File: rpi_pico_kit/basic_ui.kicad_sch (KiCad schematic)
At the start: 30 parts, among them Q3 BSS138, Q4 BSS138, Q5 BSS138, Q6 BSS138, SW2 RotaryEncoder_Switch

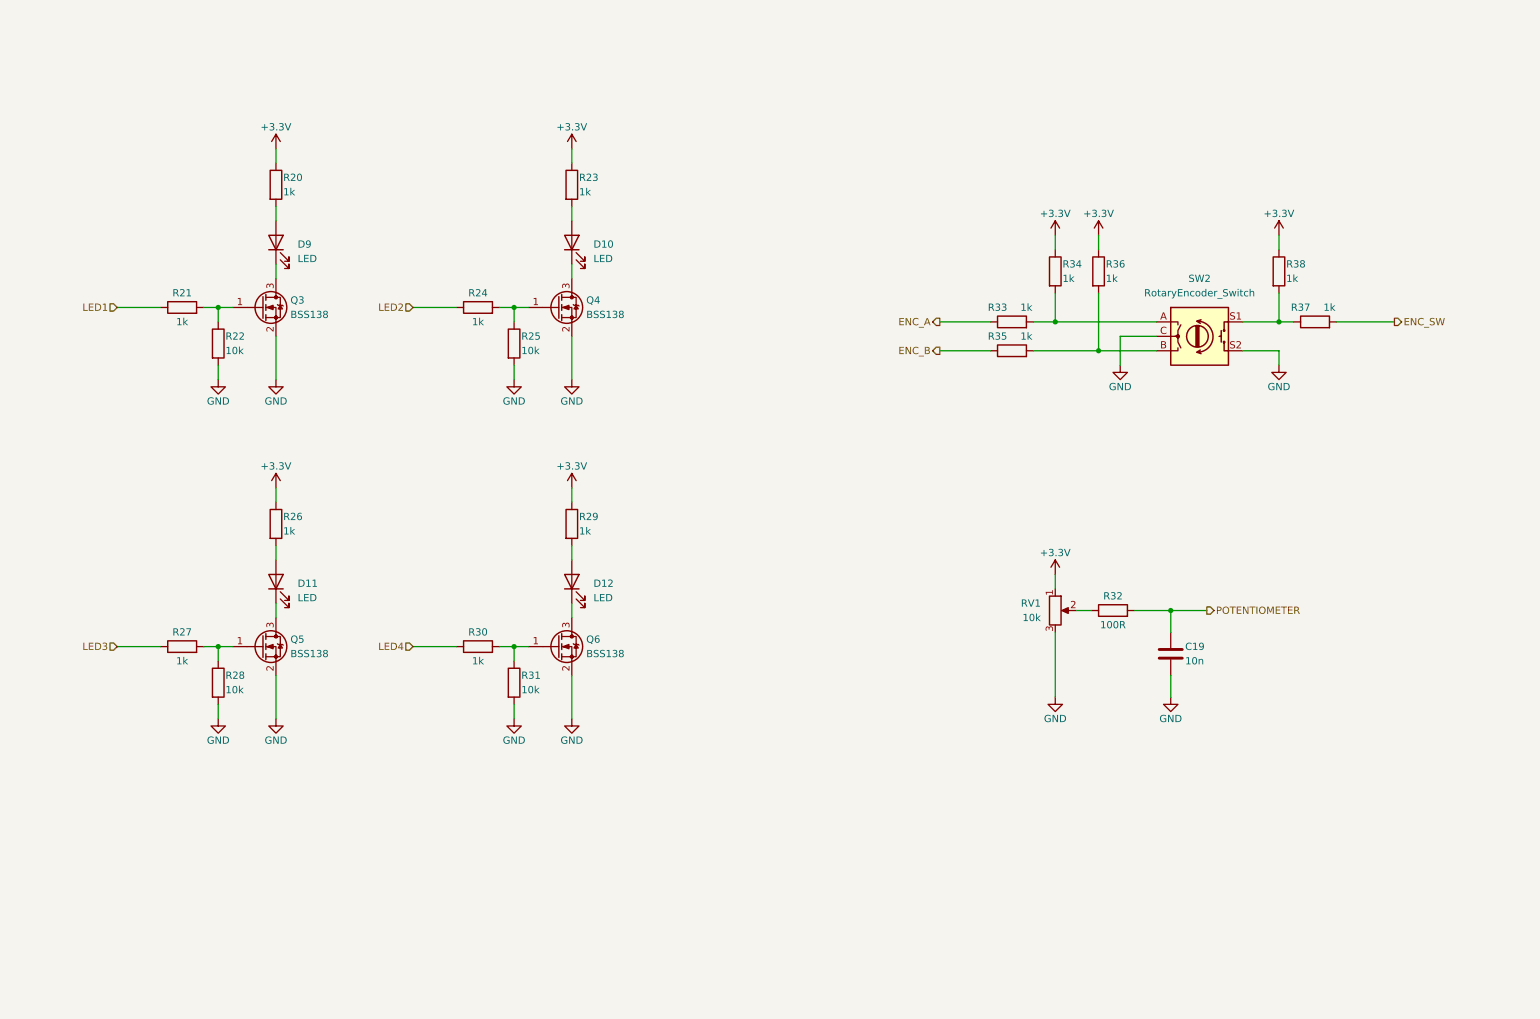
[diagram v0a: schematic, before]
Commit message: added dac buttons
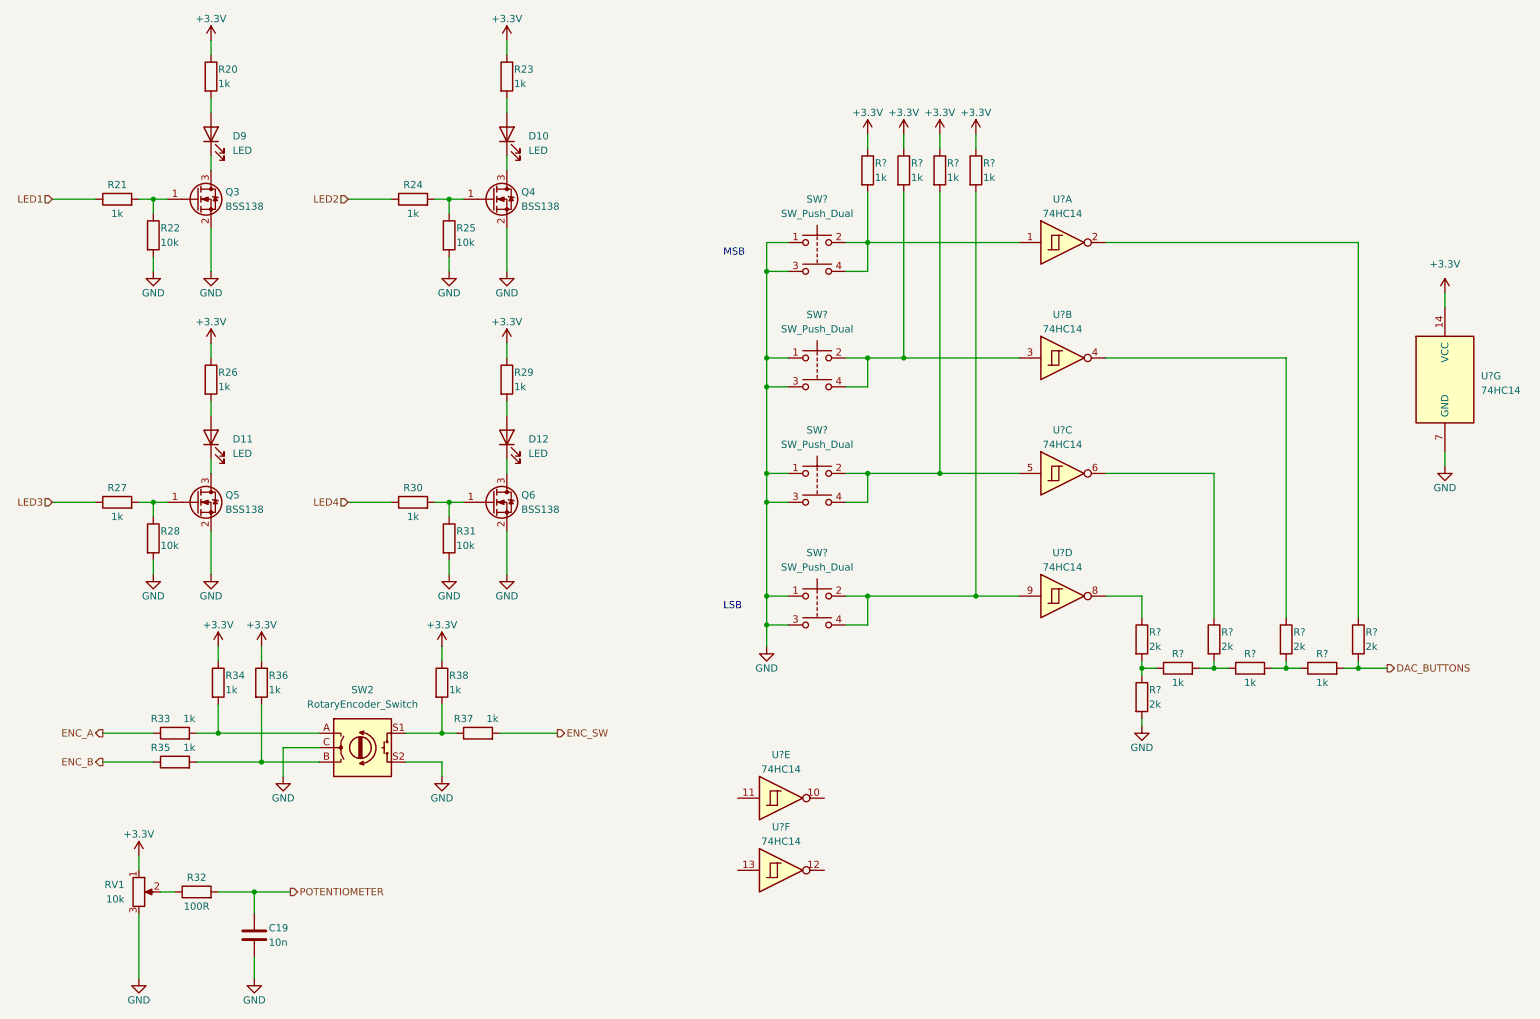
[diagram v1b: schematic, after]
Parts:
- added R? (x5): 2k, Resistor_SMD:R_0805_2012Metric_Pad1.20x1.40mm_HandSolder, symbol Device:R
- added R? (x7): 1k, Resistor_SMD:R_0805_2012Metric_Pad1.20x1.40mm_HandSolder, symbol Device:R
- added SW? (x4): SW_Push_Dual, symbol Switch:SW_Push_Dual
- added U? (x7): 74HC14, symbol 74xx:74HC14
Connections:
- net +3V3: now also R?.1, R?.1, R?.1, R?.1, U?.14 (VCC)
- net GND: now also R?.2, SW?.1, SW?.1, SW?.1, SW?.1, SW?.3, SW?.3, SW?.3, SW?.3, U?.7 (GND)
- new net: R?.2, SW?.2, SW?.4, U?.9
- new net: R?.1, U?.6
- new net: R?.1, R?.2, R?.2 (x2)
- new net: R?.2, SW?.2, SW?.4, U?.3
- new net: R?.1, U?.4
- new net: R?.1, R?.1, R?.2
- new net: R?.1, U?.8
- new net: R?.2, SW?.2, SW?.4, U?.1
- new net: R?.2, SW?.2, SW?.4, U?.5
- new net: R?.1, U?.2
- new net DAC_BUTTONS: R?.2, R?.2
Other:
- note added: "LSB"
- note added: "MSB"
- moved on the sheet: C19, D10, D11, D12, D9, Q3, Q4, Q5, Q6, R20, R21, R22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

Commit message: replaced spi expander
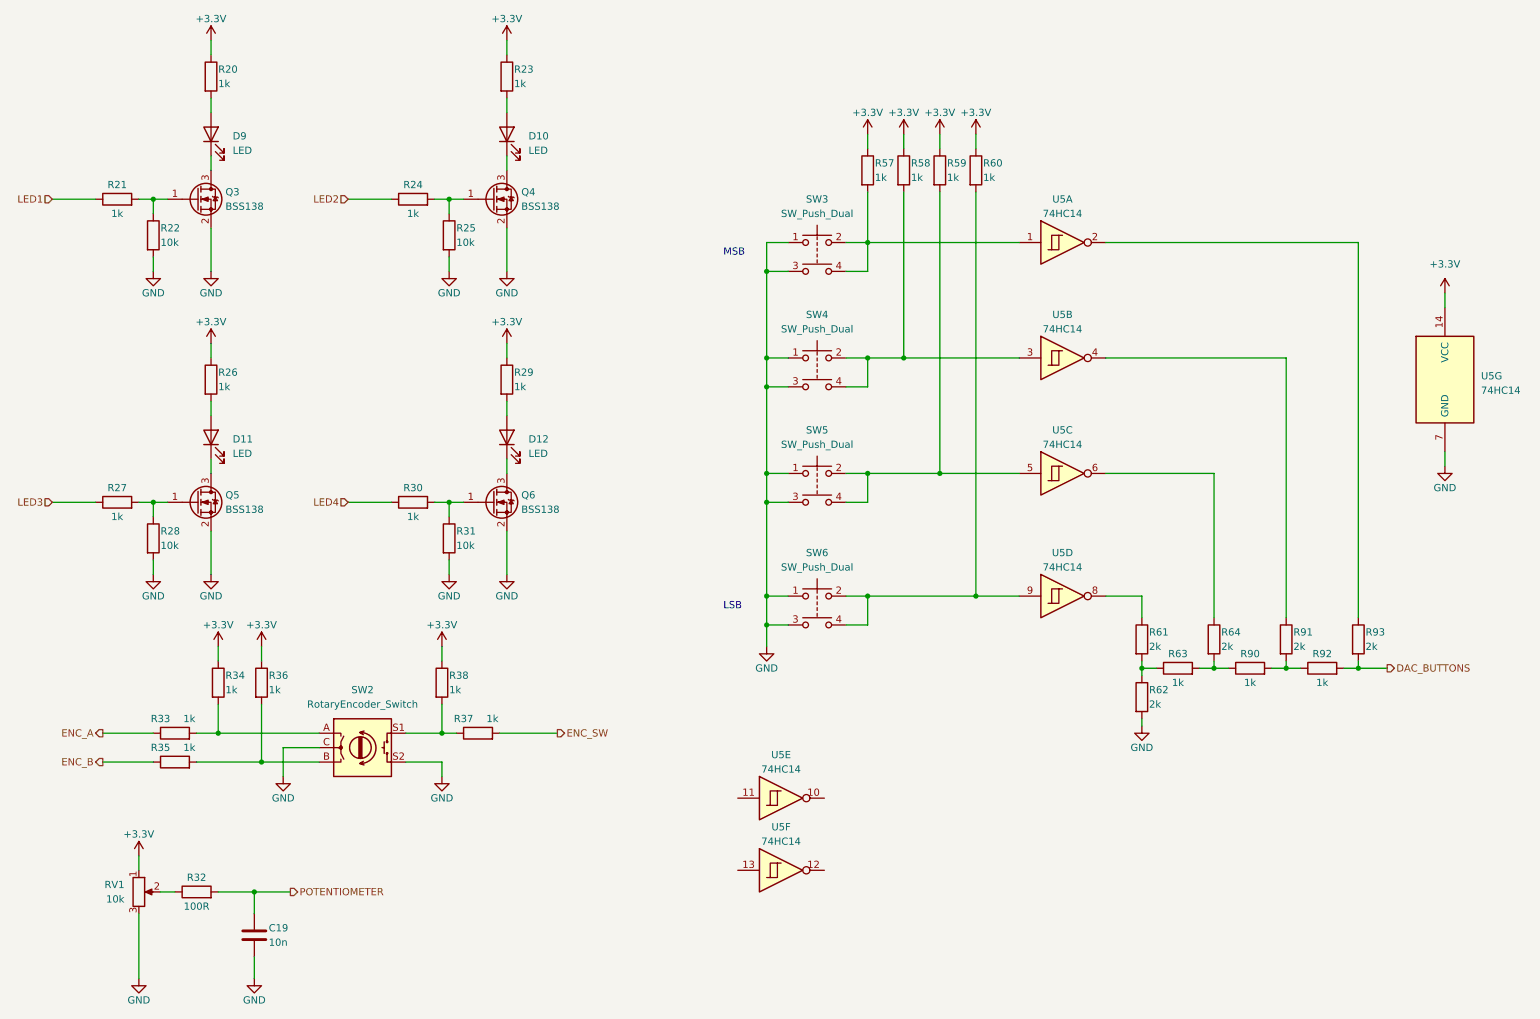
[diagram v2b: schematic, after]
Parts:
- gave numbers to parts that had none: 17
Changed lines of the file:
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@@
   (symbol (lib_id "Switch:SW_Push_Dual") (at 157.48 118.11 0) (unit 1)
     (in_bom yes) (on_board yes) (fields_autoplaced)
-    (property "Reference" "SW?" (id 0) (at 157.48 110.49 0)
+    (property "Reference" "SW6" (id 0) (at 157.48 110.49 0)
       (effects (font (size 1.27 1.27)))
     )
@@
   (symbol (lib_id "Device:R") (at 227.33 125.73 0) (unit 1)
     (in_bom yes) (on_board yes)
-    (property "Reference" "R?" (id 0) (at 228.6 124.46 0)
+    (property "Reference" "R64" (id 0) (at 228.6 124.46 0)
       (effects (font (size 1.27 1.27)) (justify left))
     )
@@
   (symbol (lib_id "power:GND") (at 148.59 127 0) (unit 1)
     (in_bom yes) (on_board yes)
-    (property "Reference" "#PWR?" (id 0) (at 148.59 133.35 0)
+    (property "Reference" "#PWR062" (id 0) (at 148.59 133.35 0)
       (effects (font (size 1.27 1.27)) hide)
     )
@@
   (symbol (lib_id "74xx:74HC14") (at 200.66 76.2 0) (unit 2)
     (in_bom yes) (on_board yes) (fields_autoplaced)
-    (property "Reference" "U?" (id 0) (at 200.66 68.58 0)
+    (property "Reference" "U5" (id 0) (at 200.66 68.58 0)
       (effects (font (size 1.27 1.27)))
     )
@@
   (symbol (lib_id "Device:R") (at 220.98 130.81 90) (unit 1)
     (in_bom yes) (on_board yes)
-    (property "Reference" "R?" (id 0) (at 220.98 128.27 90)
+    (property "Reference" "R63" (id 0) (at 220.98 128.27 90)
       (effects (font (size 1.27 1.27)))
     )
@@
   (symbol (lib_id "Device:R") (at 214.63 125.73 0) (unit 1)
     (in_bom yes) (on_board yes)
-    (property "Reference" "R?" (id 0) (at 215.9 124.46 0)
+    (property "Reference" "R61" (id 0) (at 215.9 124.46 0)
       (effects (font (size 1.27 1.27)) (justify left))
     )
@@
   (symbol (lib_id "Device:R") (at 246.38 130.81 90) (unit 1)
     (in_bom yes) (on_board yes)
-    (property "Reference" "R?" (id 0) (at 246.38 128.27 90)
+    (property "Reference" "R92" (id 0) (at 246.38 128.27 90)
       (effects (font (size 1.27 1.27)))
     )
@@
   (symbol (lib_id "power:+3.3V") (at 185.42 36.83 0) (unit 1)
     (in_bom yes) (on_board yes)
-    (property "Reference" "#PWR?" (id 0) (at 185.42 40.64 0)
+    (property "Reference" "#PWR066" (id 0) (at 185.42 40.64 0)
       (effects (font (size 1.27 1.27)) hide)
     )
@@
   (symbol (lib_id "Device:R") (at 172.72 43.18 0) (unit 1)
     (in_bom yes) (on_board yes)
-    (property "Reference" "R?" (id 0) (at 173.99 41.91 0)
+    (property "Reference" "R58" (id 0) (at 173.99 41.91 0)
       (effects (font (size 1.27 1.27)) (justify left))
     )
@@
   (symbol (lib_id "Switch:SW_Push_Dual") (at 157.48 55.88 0) (unit 1)
     (in_bom yes) (on_board yes) (fields_autoplaced)
-    (property "Reference" "SW?" (id 0) (at 157.48 48.26 0)
+    (property "Reference" "SW3" (id 0) (at 157.48 48.26 0)
       (effects (font (size 1.27 1.27)))
     )
@@
   (symbol (lib_id "Device:R") (at 166.37 43.18 0) (unit 1)
     (in_bom yes) (on_board yes)
-    (property "Reference" "R?" (id 0) (at 167.64 41.91 0)
+    (property "Reference" "R57" (id 0) (at 167.64 41.91 0)
       (effects (font (size 1.27 1.27)) (justify left))
     )
@@
   (symbol (lib_id "Device:R") (at 214.63 135.89 0) (unit 1)
     (in_bom yes) (on_board yes)
-    (property "Reference" "R?" (id 0) (at 215.9 134.62 0)
+    (property "Reference" "R62" (id 0) (at 215.9 134.62 0)
       (effects (font (size 1.27 1.27)) (justify left))
     )
@@
   (symbol (lib_id "power:+3.3V") (at 166.37 36.83 0) (unit 1)
     (in_bom yes) (on_board yes)
-    (property "Reference" "#PWR?" (id 0) (at 166.37 40.64 0)
+    (property "Reference" "#PWR063" (id 0) (at 166.37 40.64 0)
       (effects (font (size 1.27 1.27)) hide)
     )
@@
   (symbol (lib_id "power:GND") (at 267.97 95.25 0) (unit 1)
     (in_bom yes) (on_board yes)
-    (property "Reference" "#PWR?" (id 0) (at 267.97 101.6 0)
+    (property "Reference" "#PWR069" (id 0) (at 267.97 101.6 0)
       (effects (font (size 1.27 1.27)) hide)
     )
@@
   (symbol (lib_id "power:+3.3V") (at 172.72 36.83 0) (unit 1)
     (in_bom yes) (on_board yes)
-    (property "Reference" "#PWR?" (id 0) (at 172.72 40.64 0)
+    (property "Reference" "#PWR064" (id 0) (at 172.72 40.64 0)
       (effects (font (size 1.27 1.27)) hide)
     )
@@
   (symbol (lib_id "Device:R") (at 240.03 125.73 0) (unit 1)
     (in_bom yes) (on_board yes)
-    (property "Reference" "R?" (id 0) (at 241.3 124.46 0)
+    (property "Reference" "R91" (id 0) (at 241.3 124.46 0)
       (effects (font (size 1.27 1.27)) (justify left))
     )
@@
   (symbol (lib_id "power:+3.3V") (at 267.97 64.77 0) (unit 1)
     (in_bom yes) (on_board yes) (fields_autoplaced)
-    (property "Reference" "#PWR?" (id 0) (at 267.97 68.58 0)
+    (property "Reference" "#PWR068" (id 0) (at 267.97 68.58 0)
       (effects (font (size 1.27 1.27)) hide)
     )
@@
   (symbol (lib_id "Switch:SW_Push_Dual") (at 157.48 96.52 0) (unit 1)
     (in_bom yes) (on_board yes) (fields_autoplaced)
-    (property "Reference" "SW?" (id 0) (at 157.48 88.9 0)
+    (property "Reference" "SW5" (id 0) (at 157.48 88.9 0)
       (effects (font (size 1.27 1.27)))
     )
@@
   (symbol (lib_id "74xx:74HC14") (at 151.13 153.67 0) (unit 5)
     (in_bom yes) (on_board yes) (fields_autoplaced)
-    (property "Reference" "U?" (id 0) (at 151.13 146.05 0)
+    (property "Reference" "U5" (id 0) (at 151.13 146.05 0)
       (effects (font (size 1.27 1.27)))
     )
@@
   (symbol (lib_id "Device:R") (at 185.42 43.18 0) (unit 1)
     (in_bom yes) (on_board yes)
-    (property "Reference" "R?" (id 0) (at 186.69 41.91 0)
+    (property "Reference" "R60" (id 0) (at 186.69 41.91 0)
       (effects (font (size 1.27 1.27)) (justify left))
     )
@@
   (symbol (lib_id "74xx:74HC14") (at 200.66 118.11 0) (unit 4)
     (in_bom yes) (on_board yes) (fields_autoplaced)
-    (property "Reference" "U?" (id 0) (at 200.66 110.49 0)
+    (property "Reference" "U5" (id 0) (at 200.66 110.49 0)
       (effects (font (size 1.27 1.27)))
     )
@@
   (symbol (lib_id "power:+3.3V") (at 179.07 36.83 0) (unit 1)
     (in_bom yes) (on_board yes)
-    (property "Reference" "#PWR?" (id 0) (at 179.07 40.64 0)
+    (property "Reference" "#PWR065" (id 0) (at 179.07 40.64 0)
       (effects (font (size 1.27 1.27)) hide)
     )
@@
   (symbol (lib_id "74xx:74HC14") (at 200.66 96.52 0) (unit 3)
     (in_bom yes) (on_board yes) (fields_autoplaced)
-    (property "Reference" "U?" (id 0) (at 200.66 88.9 0)
+    (property "Reference" "U5" (id 0) (at 200.66 88.9 0)
       (effects (font (size 1.27 1.27)))
     )
@@
   (symbol (lib_id "Device:R") (at 179.07 43.18 0) (unit 1)
     (in_bom yes) (on_board yes)
-    (property "Reference" "R?" (id 0) (at 180.34 41.91 0)
+    (property "Reference" "R59" (id 0) (at 180.34 41.91 0)
       (effects (font (size 1.27 1.27)) (justify left))
     )
@@
   (symbol (lib_id "Switch:SW_Push_Dual") (at 157.48 76.2 0) (unit 1)
     (in_bom yes) (on_board yes) (fields_autoplaced)
-    (property "Reference" "SW?" (id 0) (at 157.48 68.58 0)
+    (property "Reference" "SW4" (id 0) (at 157.48 68.58 0)
       (effects (font (size 1.27 1.27)))
     )
@@
   (symbol (lib_id "74xx:74HC14") (at 200.66 55.88 0) (unit 1)
     (in_bom yes) (on_board yes) (fields_autoplaced)
-    (property "Reference" "U?" (id 0) (at 200.66 48.26 0)
+    (property "Reference" "U5" (id 0) (at 200.66 48.26 0)
       (effects (font (size 1.27 1.27)))
     )
@@
   (symbol (lib_id "Device:R") (at 252.73 125.73 0) (unit 1)
     (in_bom yes) (on_board yes)
-    (property "Reference" "R?" (id 0) (at 254 124.46 0)
+    (property "Reference" "R93" (id 0) (at 254 124.46 0)
       (effects (font (size 1.27 1.27)) (justify left))
     )
@@
   (symbol (lib_id "74xx:74HC14") (at 151.13 166.37 0) (unit 6)
     (in_bom yes) (on_board yes) (fields_autoplaced)
-    (property "Reference" "U?" (id 0) (at 151.13 158.75 0)
+    (property "Reference" "U5" (id 0) (at 151.13 158.75 0)
       (effects (font (size 1.27 1.27)))
     )
@@
   (symbol (lib_id "Device:R") (at 233.68 130.81 90) (unit 1)
     (in_bom yes) (on_board yes)
-    (property "Reference" "R?" (id 0) (at 233.68 128.27 90)
+    (property "Reference" "R90" (id 0) (at 233.68 128.27 90)
       (effects (font (size 1.27 1.27)))
     )
@@
   (symbol (lib_id "power:GND") (at 214.63 140.97 0) (unit 1)
     (in_bom yes) (on_board yes)
-    (property "Reference" "#PWR?" (id 0) (at 214.63 147.32 0)
+    (property "Reference" "#PWR067" (id 0) (at 214.63 147.32 0)
       (effects (font (size 1.27 1.27)) hide)
     )
@@
   (symbol (lib_id "74xx:74HC14") (at 267.97 80.01 0) (unit 7)
     (in_bom yes) (on_board yes) (fields_autoplaced)
-    (property "Reference" "U?" (id 0) (at 274.32 79.375 0)
-      (effects (font (size 1.27 1.27)) (justify left))
-    )
+    (property "Reference" "U5" (id 0) (at 274.32 79.375 0)
+      (effects (font (size 1.27 1.27)) (justify left))
+    )
